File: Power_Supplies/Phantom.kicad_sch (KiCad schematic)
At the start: 14 parts, among them IC9 LT8338

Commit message: Add files via upload
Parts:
- removed C116, C117: 220uF, Capacitor_SMD:C_0402_1005Metric, symbol Device:C
- removed R46, R47: 10k, Resistor_SMD:R_0805_2012Metric, symbol Device:R
- added C102, C107: 22uF, Capacitor_SMD:CP_Elec_4x5.8, symbol Device:C_Polarized_US
- added C32: 10uF, Capacitor_SMD:CP_Elec_4x5.8, symbol Device:C_Polarized_US
- added D1: LED, LED_SMD:LED_0201_0603Metric, symbol PCM_SL_Devices:LED
- added DZ1, DZ2, DZ3, DZ4: 10V, Diode_SMD:D_SMB, symbol PCM_Diode_Zener_AKL:D_Zener_Generic
- added J8: XLR3, symbol Connector_Audio:XLR3
- added R30, R31: 5.1k, Resistor_SMD:R_0805_2012Metric, symbol Device:R
- added R32, R33: 10, Resistor_SMD:R_0805_2012Metric, symbol Device:R
- added R45: 2.2k, Resistor_SMD:R_0805_2012Metric, symbol Device:R
- added SW1: SW_Push, Button_Switch_THT:SW_PUSH_1P1T_6x3.5mm_H5.0_APEM_MJTP1250, symbol Switch:SW_Push
- IC9: footprint SOP50P490X110-11N -> SamacSys_Parts:SOP65P490X110-9N
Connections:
- net 36V: now also SW1.2
- net AGND: now also C32.2, DZ3.2 (A), DZ4.2 (A), J8.1, R45.2
- new net: DZ2.1 (K), DZ4.1 (K)
- new net: C107.2, R33.1
- new net: C32.1, D1.2, R30.1, R31.1, SW1.1
- new net: C107.1, J8.3, R31.2
- new net: D1.1, R45.1
- new net: C102.1, J8.2, R30.2
- new net: C102.2, R32.1
- new net: DZ1.1 (K), DZ3.1 (K)
- new net +IN: DZ2.2 (A), R32.2
- new net -IN: DZ1.2 (A), R33.2
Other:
- note added: "Negative"
- note added: "Phantom Power Circuit"
- note added: "Phantom Power Enable"
- note added: "Positive"
- note added: "To Mic Preamp"
- note removed: "Virtual Ground"

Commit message: Finished HiZ Inputs
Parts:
- removed C102, C107: 22uF, Capacitor_SMD:CP_Elec_4x5.8, symbol Device:C_Polarized_US
- removed C32: 10uF, Capacitor_SMD:CP_Elec_4x5.8, symbol Device:C_Polarized_US
- removed D1: LED, LED_SMD:LED_0201_0603Metric, symbol PCM_SL_Devices:LED
- removed DZ1, DZ2, DZ3, DZ4: 10V, Diode_SMD:D_SMB, symbol PCM_Diode_Zener_AKL:D_Zener_Generic
- removed J8: XLR3, symbol Connector_Audio:XLR3
- removed R30, R31: 5.1k, Resistor_SMD:R_0805_2012Metric, symbol Device:R
- removed R32, R33: 10, Resistor_SMD:R_0805_2012Metric, symbol Device:R
- removed R45: 2.2k, Resistor_SMD:R_0805_2012Metric, symbol Device:R
- removed SW1: SW_Push, Button_Switch_THT:SW_PUSH_1P1T_6x3.5mm_H5.0_APEM_MJTP1250, symbol Switch:SW_Push
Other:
- note removed: "Negative"
- note removed: "Phantom Power Circuit"
- note removed: "Phantom Power Enable"
- note removed: "Positive"
- note removed: "To Mic Preamp"

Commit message: big things are coming...
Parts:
- renumbered C103 to C51, C108 to C52, C109 to C53, IC9 to IC2, R34 to R37, R35 to R38, R44 to R39, R42 to R40, R43 to R41
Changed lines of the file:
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@@
 		(dnp no)
 		(fields_autoplaced yes)
-		(property "Reference" "C108"
+		(property "Reference" "C52"
 			(at 111.76 45.72 90)
 			(effects
@@
 			(project "Power_Supplies"
 				(path "/5266cf9e-da90-4c53-80fd-cf3dbed42632/873b4819-32e6-40de-93d6-23cb6a01b934"
-					(reference "C108")
+					(reference "C52")
 					(unit 1)
 				)
@@
 		(dnp no)
 		(fields_autoplaced yes)
-		(property "Reference" "#PWR048"
+		(property "Reference" "#PWR053"
 			(at 58.42 77.47 0)
 			(effects
@@
 			(project "Power_Supplies"
 				(path "/5266cf9e-da90-4c53-80fd-cf3dbed42632/873b4819-32e6-40de-93d6-23cb6a01b934"
-					(reference "#PWR048")
+					(reference "#PWR053")
 					(unit 1)
 				)
@@
 		(dnp no)
 		(fields_autoplaced yes)
-		(property "Reference" "#PWR053"
+		(property "Reference" "#PWR056"
 			(at 123.19 81.28 0)
 			(effects
@@
 			(project "Power_Supplies"
 				(path "/5266cf9e-da90-4c53-80fd-cf3dbed42632/873b4819-32e6-40de-93d6-23cb6a01b934"
-					(reference "#PWR053")
+					(reference "#PWR056")
 					(unit 1)
 				)
@@
 		(on_board yes)
 		(dnp no)
-		(property "Reference" "#PWR050"
+		(property "Reference" "#PWR057"
 			(at 132.08 72.39 0)
 			(effects
@@
 			(project "Power_Supplies"
 				(path "/5266cf9e-da90-4c53-80fd-cf3dbed42632/873b4819-32e6-40de-93d6-23cb6a01b934"
-					(reference "#PWR050")
+					(reference "#PWR057")
 					(unit 1)
 				)
@@
 		(dnp no)
 		(fields_autoplaced yes)
-		(property "Reference" "R34"
+		(property "Reference" "R37"
 			(at 60.96 55.8799 0)
 			(effects
@@
 			(project "Power_Supplies"
 				(path "/5266cf9e-da90-4c53-80fd-cf3dbed42632/873b4819-32e6-40de-93d6-23cb6a01b934"
-					(reference "R34")
+					(reference "R37")
 					(unit 1)
 				)
@@
 		(dnp no)
 		(fields_autoplaced yes)
-		(property "Reference" "C109"
+		(property "Reference" "C53"
 			(at 135.89 62.2299 0)
 			(effects
@@
 			(project "Power_Supplies"
 				(path "/5266cf9e-da90-4c53-80fd-cf3dbed42632/873b4819-32e6-40de-93d6-23cb6a01b934"
-					(reference "C109")
+					(reference "C53")
 					(unit 1)
 				)
@@
 		(dnp no)
 		(fields_autoplaced yes)
-		(property "Reference" "#PWR052"
+		(property "Reference" "#PWR055"
 			(at 116.84 80.01 0)
 			(effects
@@
 			(project "Power_Supplies"
 				(path "/5266cf9e-da90-4c53-80fd-cf3dbed42632/873b4819-32e6-40de-93d6-23cb6a01b934"
-					(reference "#PWR052")
+					(reference "#PWR055")
 					(unit 1)
 				)
@@
 		(dnp no)
 		(fields_autoplaced yes)
-		(property "Reference" "#PWR049"
+		(property "Reference" "#PWR054"
 			(at 99.06 88.9 0)
 			(effects
@@
 			(project "Power_Supplies"
 				(path "/5266cf9e-da90-4c53-80fd-cf3dbed42632/873b4819-32e6-40de-93d6-23cb6a01b934"
-					(reference "#PWR049")
+					(reference "#PWR054")
 					(unit 1)
 				)
@@
 		(dnp no)
 		(fields_autoplaced yes)
-		(property "Reference" "C103"
+		(property "Reference" "C51"
 			(at 52.07 58.4199 0)
 			(effects
@@
 			(project "Power_Supplies"
 				(path "/5266cf9e-da90-4c53-80fd-cf3dbed42632/873b4819-32e6-40de-93d6-23cb6a01b934"
-					(reference "C103")
+					(reference "C51")
 					(unit 1)
 				)
@@
 		(dnp no)
 		(fields_autoplaced yes)
-		(property "Reference" "IC9"
+		(property "Reference" "IC2"
 			(at 99.06 52.07 0)
 			(effects
@@
 			(project ""
 				(path "/5266cf9e-da90-4c53-80fd-cf3dbed42632/873b4819-32e6-40de-93d6-23cb6a01b934"
-					(reference "IC9")
+					(reference "IC2")
 					(unit 1)
 				)
@@
 		(on_board yes)
 		(dnp no)
-		(property "Reference" "R44"
+		(property "Reference" "R39"
 			(at 124.46 69.85 0)
 			(effects
@@
 			(project "Power_Supplies"
 				(path "/5266cf9e-da90-4c53-80fd-cf3dbed42632/873b4819-32e6-40de-93d6-23cb6a01b934"
-					(reference "R44")
+					(reference "R39")
 					(unit 1)
 				)
@@
 		(dnp no)
 		(fields_autoplaced yes)
-		(property "Reference" "R42"
+		(property "Reference" "R40"
 			(at 146.05 62.2299 0)
 			(effects
@@
 			(project "Power_Supplies"
 				(path "/5266cf9e-da90-4c53-80fd-cf3dbed42632/873b4819-32e6-40de-93d6-23cb6a01b934"
-					(reference "R42")
+					(reference "R40")
 					(unit 1)
 				)
@@
 		(dnp no)
 		(fields_autoplaced yes)
-		(property "Reference" "R35"
+		(property "Reference" "R38"
 			(at 60.96 66.0399 0)
 			(effects
@@
 			(project "Power_Supplies"
 				(path "/5266cf9e-da90-4c53-80fd-cf3dbed42632/873b4819-32e6-40de-93d6-23cb6a01b934"
-					(reference "R35")
+					(reference "R38")
 					(unit 1)
 				)
@@
 		(dnp no)
 		(fields_autoplaced yes)
-		(property "Reference" "#PWR051"
+		(property "Reference" "#PWR058"
 			(at 143.51 85.09 0)
 			(effects
@@
 			(project "Power_Supplies"
 				(path "/5266cf9e-da90-4c53-80fd-cf3dbed42632/873b4819-32e6-40de-93d6-23cb6a01b934"
-					(reference "#PWR051")
+					(reference "#PWR058")
 					(unit 1)
 				)
@@
 		(dnp no)
 		(fields_autoplaced yes)
-		(property "Reference" "R43"
+		(property "Reference" "R41"
 			(at 146.05 73.6599 0)
 			(effects
@@
 			(project "Power_Supplies"
 				(path "/5266cf9e-da90-4c53-80fd-cf3dbed42632/873b4819-32e6-40de-93d6-23cb6a01b934"
-					(reference "R43")
+					(reference "R41")
 					(unit 1)
 				)
@@
 		(dnp no)
 		(fields_autoplaced yes)
-		(property "Reference" "#PWR047"
+		(property "Reference" "#PWR052"
 			(at 48.26 69.85 0)
 			(effects
@@
 			(project "Power_Supplies"
 				(path "/5266cf9e-da90-4c53-80fd-cf3dbed42632/873b4819-32e6-40de-93d6-23cb6a01b934"
-					(reference "#PWR047")
-					(unit 1)
-				)
+					(reference "#PWR052")
+					(unit 1)
+				)

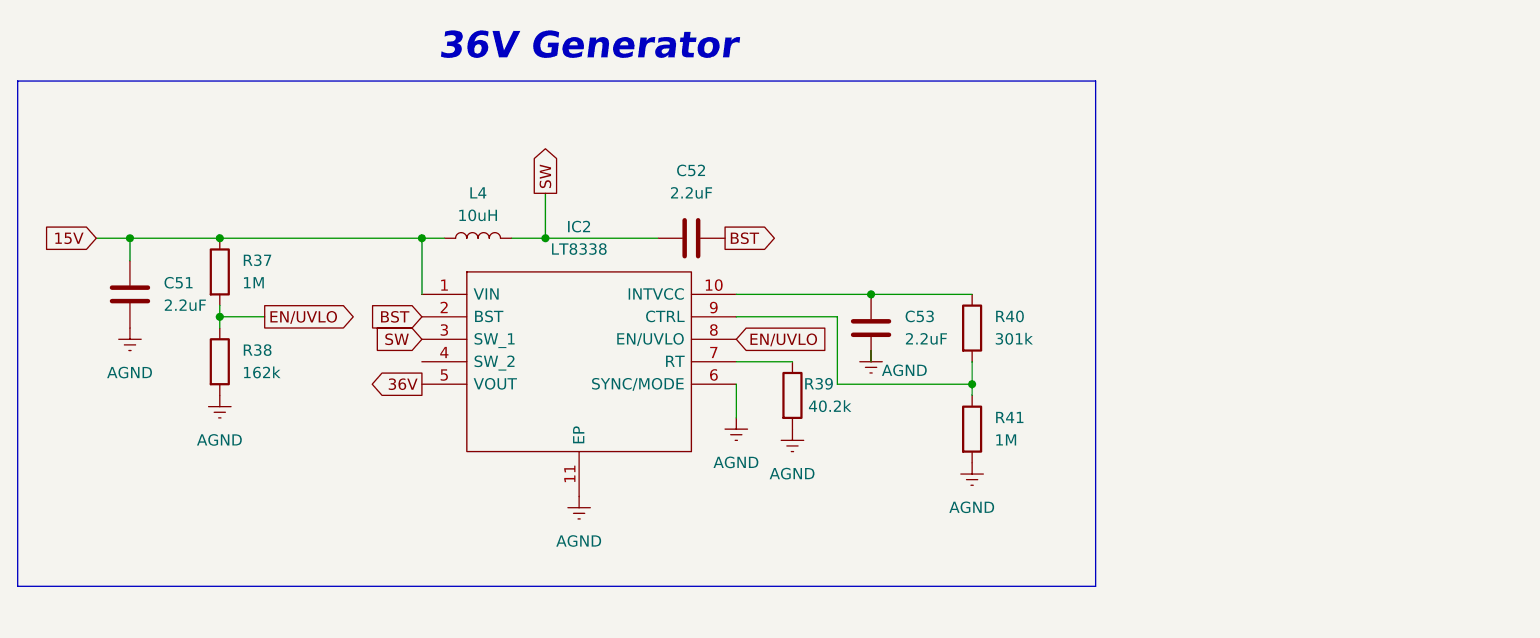
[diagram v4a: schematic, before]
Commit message: added both ADCs, added differential output to DACs
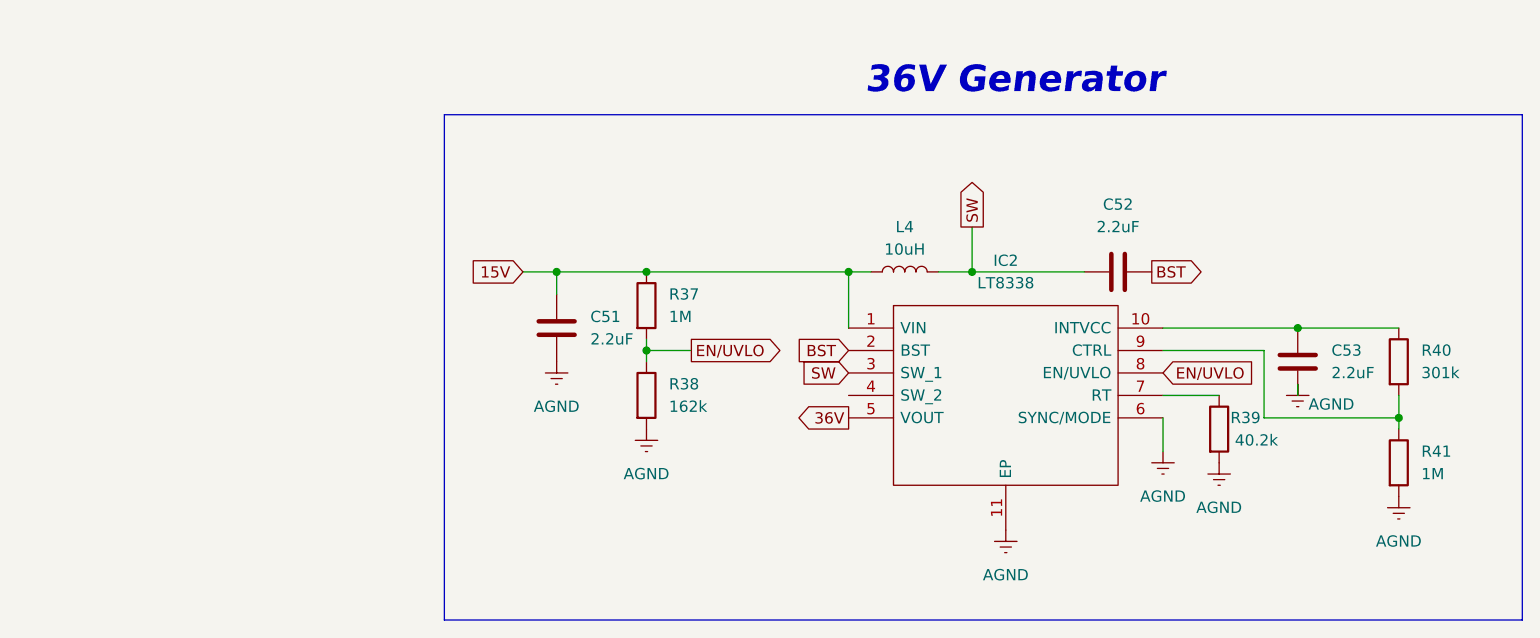
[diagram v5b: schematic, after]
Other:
- moved on the sheet: C51, C52, C53, IC2, L4, R37, R38, R39, R40, R41

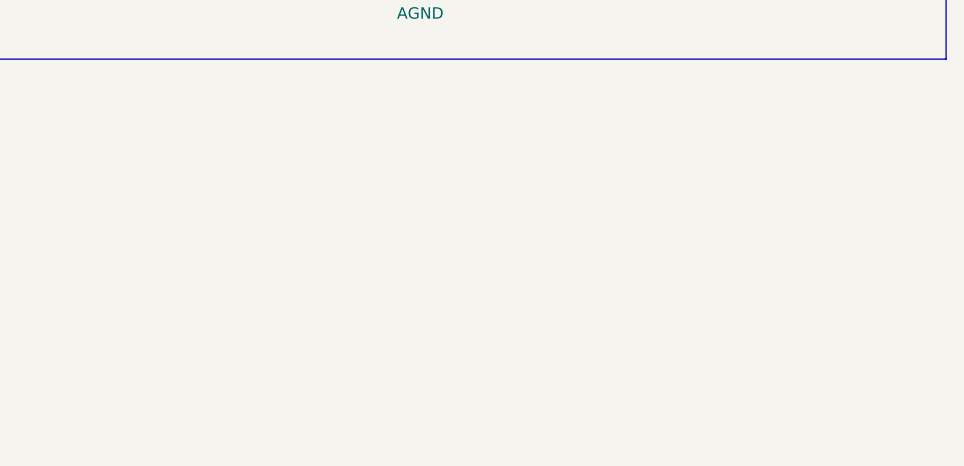
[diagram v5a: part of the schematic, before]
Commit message: Added BIG KNOB schematic and started PCB
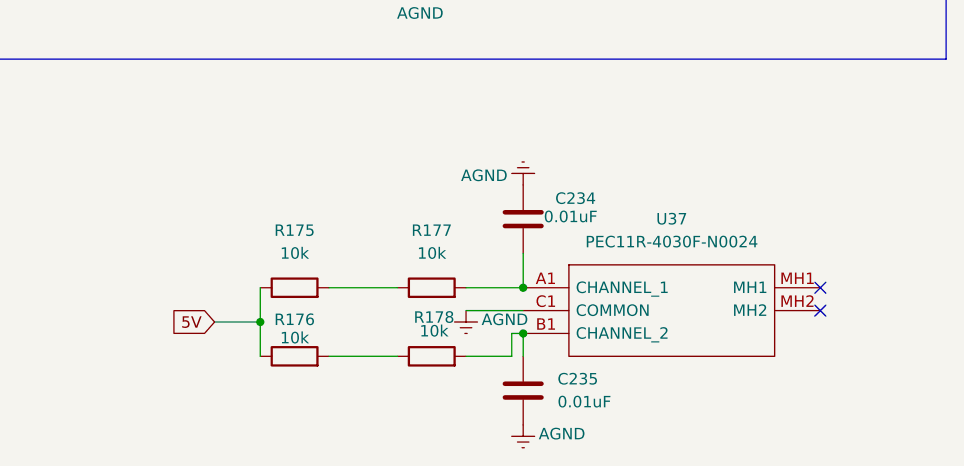
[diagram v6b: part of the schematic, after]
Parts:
- added C234, C235: 0.01uF, Capacitor_SMD:C_0402_1005Metric, symbol Device:C
- added R175, R176, R177, R178: 10k, Resistor_SMD:R_0805_2012Metric, symbol Device:R
- added U37: PEC11R-4030F-N0024, PEC11R4030FN0024, symbol SamacSys_Parts:PEC11R-4030F-N0024
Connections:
- net AGND: now also C234.1, C235.2, U37.C1 (COMMON)
- new net: C235.1, R178.2, U37.B1 (CHANNEL_2)
- new net: R176.2, R178.1
- new net: R175.2, R177.1
- new net: C234.2, R177.2, U37.A1 (CHANNEL_1)
- new net 5V: R175.1, R176.1
- no-connect marks 0 -> 2

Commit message: initial placement of all cmponents
need to add:
- pin headers for Rpi
- separate the boards and add pin headers for connection points
- probably get rid of buck converters and change LDOs to be higher current
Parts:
- IC2: footprint SamacSys_Parts:SOP65P490X110-9N -> SamacSys_Parts:SOP50P490X110-11N
- U37: footprint PEC11R4030FN0024 -> SamacSys_Parts:PEC11R4030FN0024
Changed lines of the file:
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@@
 			)
 		)
-		(property "Footprint" "SamacSys_Parts:SOP65P490X110-9N"
+		(property "Footprint" "SamacSys_Parts:SOP50P490X110-11N"
 			(at 161.29 60.96 0)
 			(effects
@@
 			)
 		)
-		(property "Footprint" "PEC11R4030FN0024"
+		(property "Footprint" "SamacSys_Parts:PEC11R4030FN0024"
 			(at 187.96 119.38 0)
 			(effects

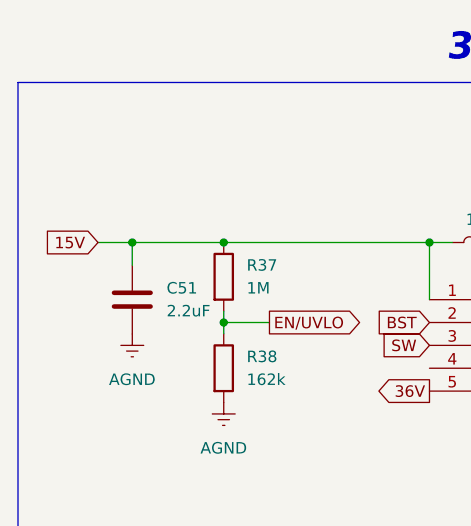
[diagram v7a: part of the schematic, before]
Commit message: Added stuff for the power supply circuitry
changed all grounds to GND (same ground plane)
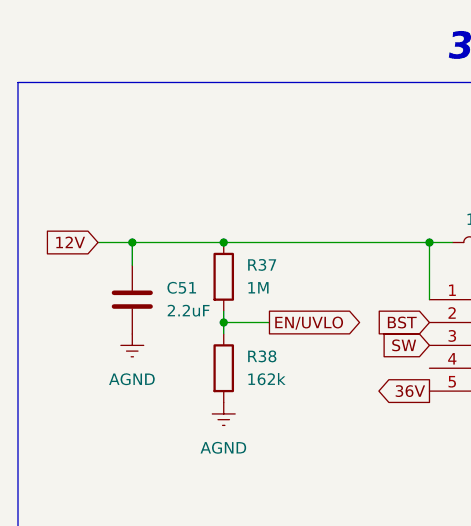
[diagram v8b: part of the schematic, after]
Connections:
- net 15V renamed 12V
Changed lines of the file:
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@@
 		)
 	)
-	(global_label "15V"
+	(global_label "12V"
 		(shape input)
 		(at 92.71 57.15 180)
@@
 		(exclude_from_sim no)
 		(in_bom yes)
-		(on_board yes)
+		(on_board no)
 		(dnp no)
 		(property "Reference" "C235"
@@
 		(exclude_from_sim no)
 		(in_bom yes)
-		(on_board yes)
+		(on_board no)
 		(dnp no)
 		(property "Reference" "R176"
@@
 		(exclude_from_sim no)
 		(in_bom yes)
-		(on_board yes)
+		(on_board no)
 		(dnp no)
 		(property "Reference" "R178"
@@
 		(exclude_from_sim no)
 		(in_bom yes)
-		(on_board yes)
+		(on_board no)
 		(dnp no)
 		(fields_autoplaced yes)
@@
 		(exclude_from_sim no)
 		(in_bom yes)
-		(on_board yes)
+		(on_board no)
 		(dnp no)
 		(property "Reference" "C234"
@@
 		(exclude_from_sim no)
 		(in_bom yes)
-		(on_board yes)
+		(on_board no)
 		(dnp no)
 		(fields_autoplaced yes)
@@
 		(exclude_from_sim no)
 		(in_bom yes)
-		(on_board yes)
+		(on_board no)
 		(dnp no)
 		(property "Reference" "#PWR0225"
@@
 		(exclude_from_sim no)
 		(in_bom yes)
-		(on_board yes)
+		(on_board no)
 		(dnp no)
 		(property "Reference" "#PWR0224"
@@
 		(exclude_from_sim no)
 		(in_bom yes)
-		(on_board yes)
+		(on_board no)
 		(dnp no)
 		(property "Reference" "#PWR0223"
@@
 		(exclude_from_sim no)
 		(in_bom yes)
-		(on_board yes)
+		(on_board no)
 		(dnp no)
 		(fields_autoplaced yes)
